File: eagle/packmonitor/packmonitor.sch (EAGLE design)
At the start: 35 parts, among them IC1 24C64, IC2 TCA4311A, IC3 AP2411, IC4 ACS712, Q1 PCHAN, X1 JST-XH-06-PIN-LONG-PAD

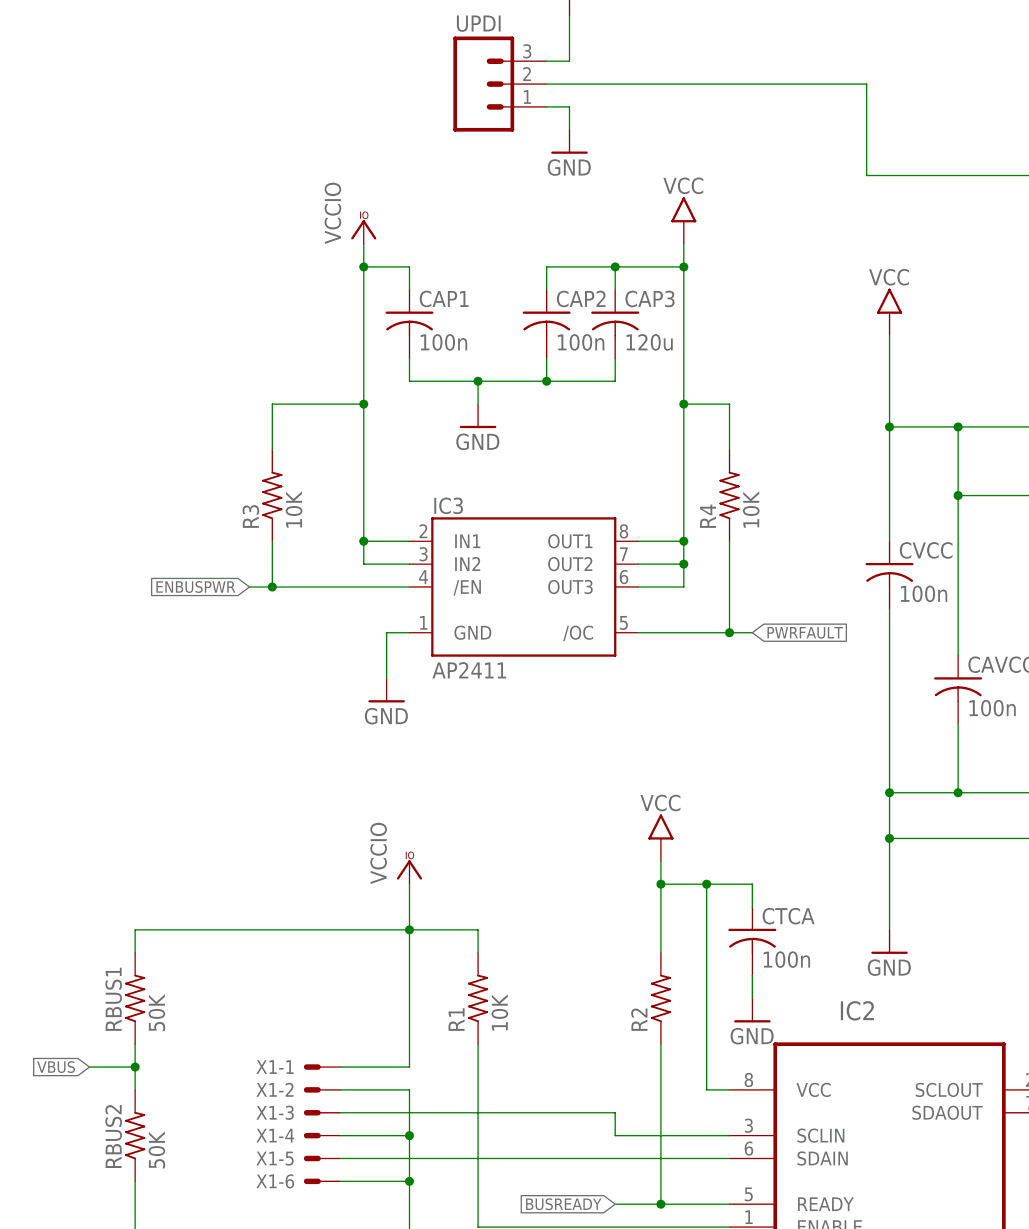
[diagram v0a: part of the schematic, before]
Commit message: got rid of input power switch
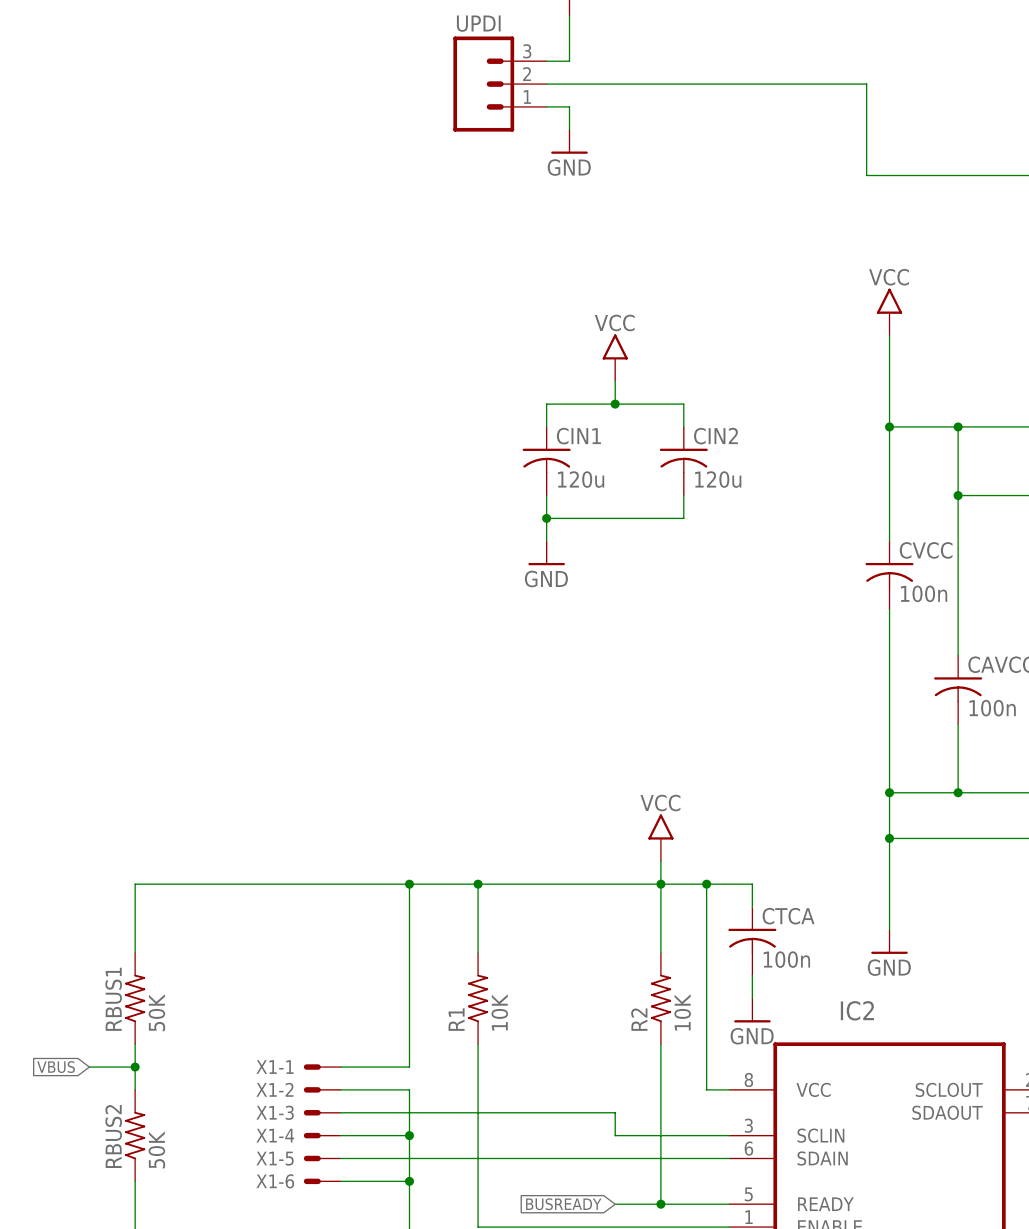
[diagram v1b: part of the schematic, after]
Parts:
- removed CAP1, CAP2: 100n, rcl:C-USC0603
- removed CAP3: 120u, rcl:C-USC1206
- removed IC3: AP2411, ti-special:TPS2041BD
- removed R3, R4: 10K, rcl:R-US_R0603
- added CIN1, CIN2: 120u, rcl:C-USC1206
- R2: value (none) -> 10K
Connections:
- removed net ENBUSPWR: IC3./EN, R3.1
- removed net PWRFAULT: IC3./OC, R4.1
- removed net VCCIO: CAP1.1, IC3.IN1, IC3.IN2, R1.2, R3.2, RBUS1.2, X1-1.S
- net GND: now also CIN1.2, CIN2.2; no longer CAP1.2, CAP2.2, CAP3.2, IC3.GND
- net VCC: now also CIN1.1, CIN2.1, R1.2, RBUS1.2, X1-1.S; no longer CAP2.1, CAP3.1, IC3.OUT1, IC3.OUT2, IC3.OUT3, R4.2

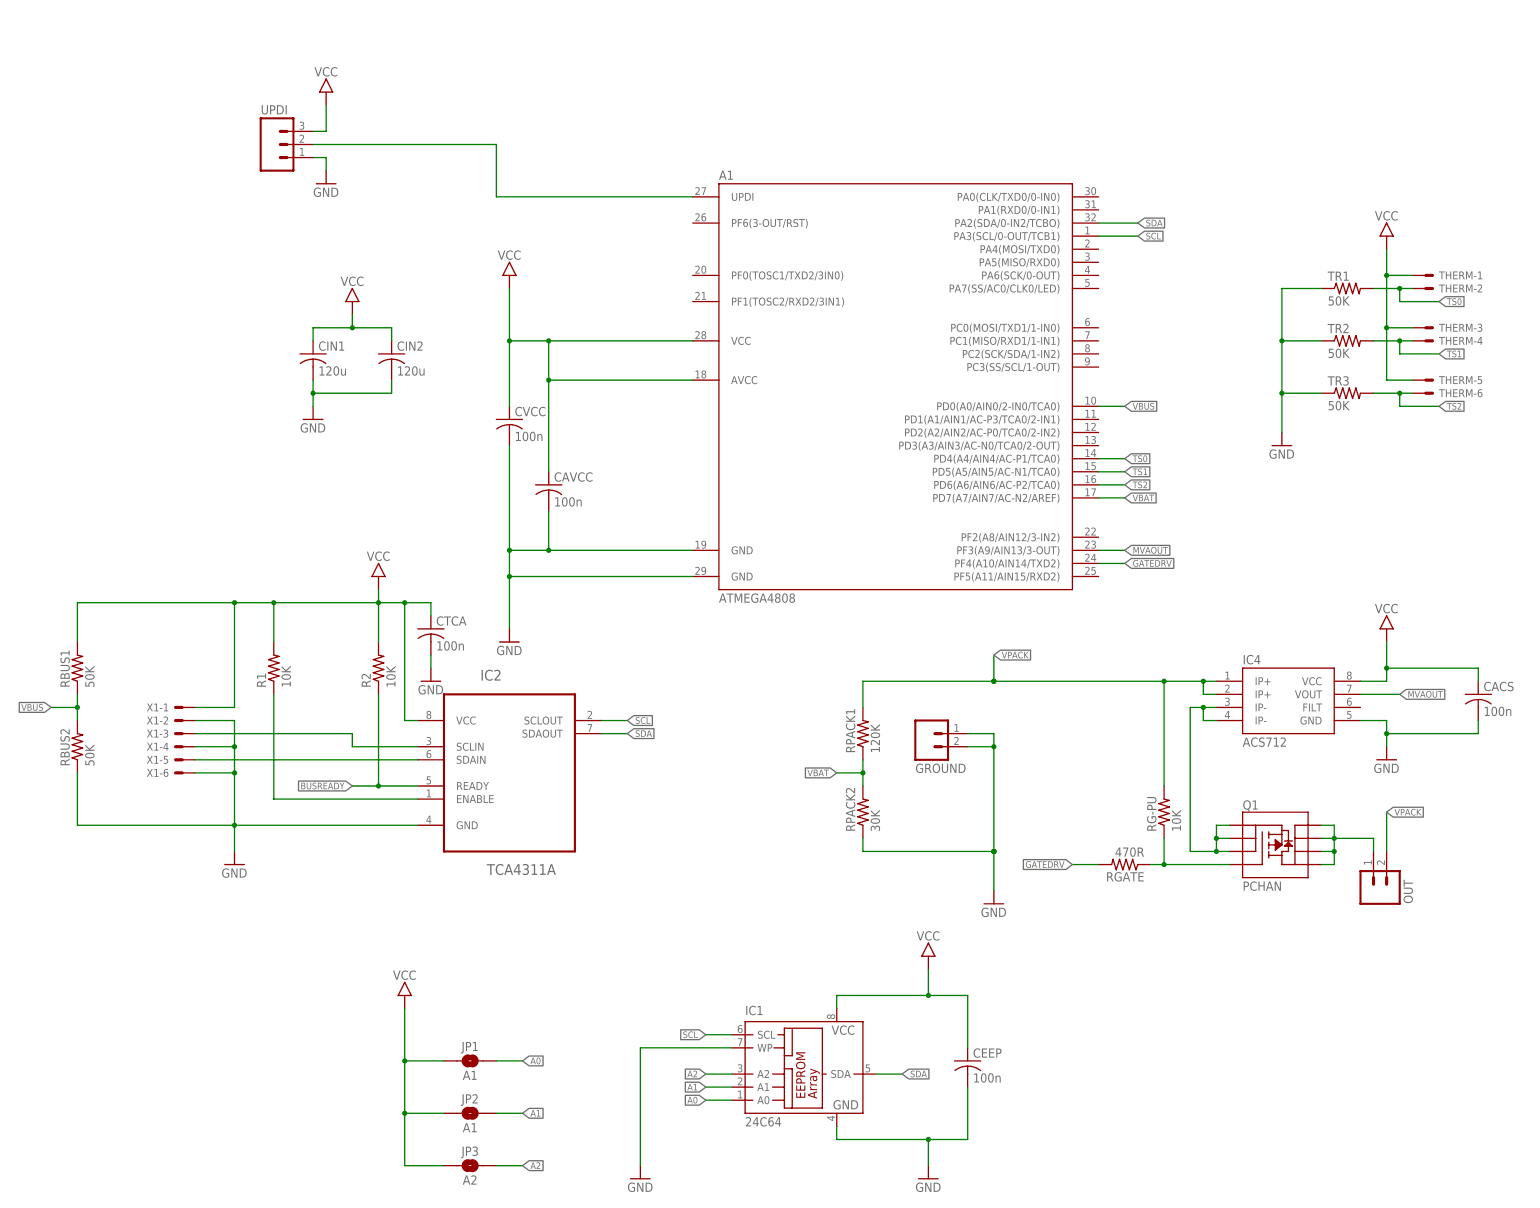
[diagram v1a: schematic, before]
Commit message: switched to avr128da32 chip & low side disconnect
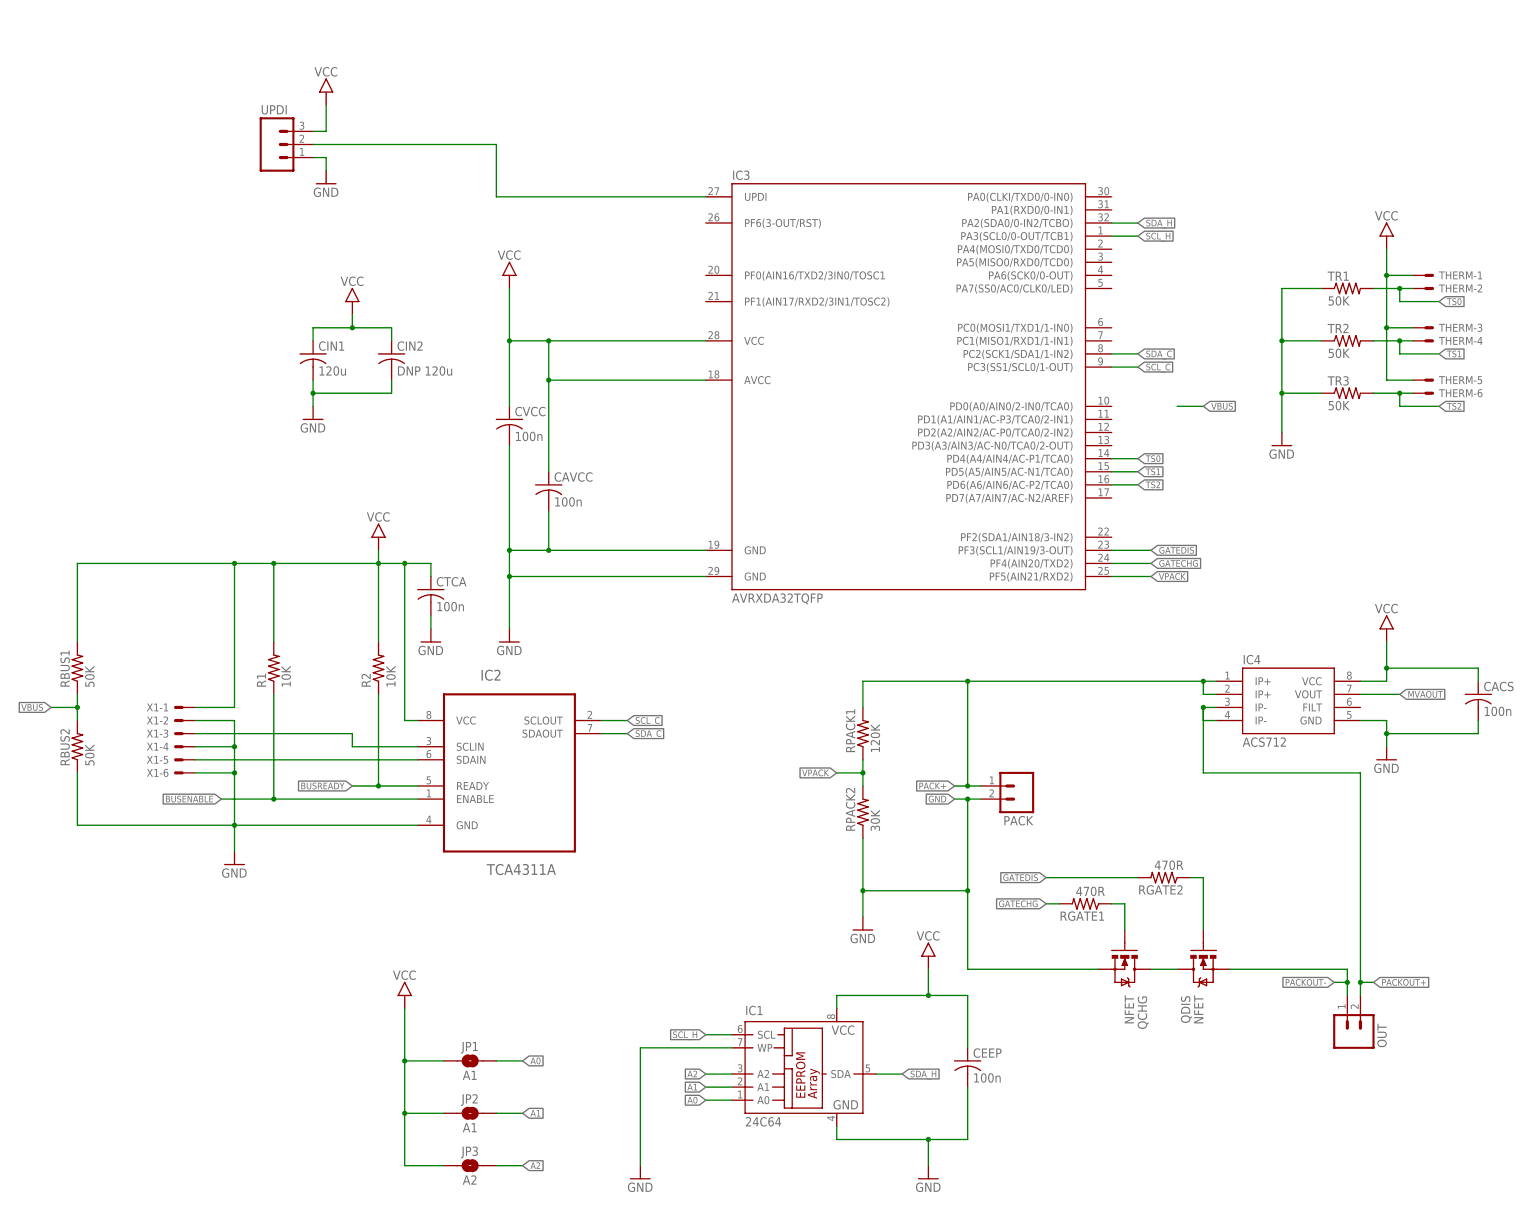
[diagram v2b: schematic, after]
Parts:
- removed A1: ATMEGA4808, microchip-special:ATMEGA4808-TQFN32A
- removed GROUND: (no value), SparkFun-Connectors:M023.5MM
- removed Q1: PCHAN, SparkFun-DiscreteSemi:MOSFET-PCHANNEL-SOIC8SOIC8
- removed RG-PU: 10K, rcl:R-US_R0603
- removed RGATE: 470R, rcl:R-US_R0603
- added IC3: AVRXDA32TQFP, microchip-special:AVRXDA32TQFP
- added PACK: (no value), SparkFun-Connectors:M023.5MM
- added QCHG, QDIS: NFET, SparkFun-DiscreteSemi:MOSFET-NCHANNELFDS6630A
- added RGATE1, RGATE2: 470R, rcl:R-US_R0603
- CIN2: value 120u -> DNP 120u
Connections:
- net N$6 renamed BUSENABLE
- removed net GATE: Q1.G, RG-PU.1, RGATE.1
- removed net GATEDRV: A1.PF4(A10/AIN14/TXD2), RGATE.2
- removed net P+IN: IC4.IP-@3, IC4.IP-@4, Q1.S@1, Q1.S@2, Q1.S@3
- removed net P+OUT: OUT.1, Q1.D@1, Q1.D@2, Q1.D@3, Q1.D@4
- removed net SCL: A1.PA3(SCL/0-OUT/TCB1), IC1.SCL, IC2.SCLOUT
- removed net SDA: A1.PA2(SDA/0-IN2/TCBO), IC1.SDA, IC2.SDAOUT
- removed net VBAT: A1.PD7(A7/AIN7/AC-N2/AREF), RPACK1.1, RPACK2.2
- new net GATECHG: IC3.PF4(AIN20/TXD2), RGATE1.2
- new net GATEDIS: IC3.PF3(SCL1/AIN19/3-OUT), RGATE2.2
- new net N$1: QCHG.G, RGATE1.1
- new net N$2: QDIS.G, RGATE2.1
- new net PACK+: IC4.IP+@1, IC4.IP+@2, PACK.1, RPACK1.2
- new net PACKOUT+: IC4.IP-@3, IC4.IP-@4, OUT.2
- new net PACKOUT-: OUT.1, QDIS.S
- new net PDISC: QCHG.D, QDIS.D
- new net SCL_C: IC2.SCLOUT, IC3.PC3(SS1/SCL0/1-OUT)
- new net SCL_H: IC1.SCL, IC3.PA3(SCL0/0-OUT/TCB1)
- new net SDA_C: IC2.SDAOUT, IC3.PC2(SCK1/SDA1/1-IN2)
- new net SDA_H: IC1.SDA, IC3.PA2(SDA0/0-IN2/TCBO)
- net GND: now also IC3.GND@1, IC3.GND@2, PACK.2, QCHG.S; no longer A1.GND@1, A1.GND@2, GROUND.1, GROUND.2
- net MVAOUT: no longer A1.PF3(A9/AIN13/3-OUT)
- net TS0: now also IC3.PD4(A4/AIN4/AC-P1/TCA0); no longer A1.PD4(A4/AIN4/AC-P1/TCA0)
- net TS1: now also IC3.PD5(A5/AIN5/AC-N1/TCA0); no longer A1.PD5(A5/AIN5/AC-N1/TCA0)
- net TS2: now also IC3.PD6(A6/AIN6/AC-P2/TCA0); no longer A1.PD6(A6/AIN6/AC-P2/TCA0)
- net UPDI: now also IC3.UPDI; no longer A1.UPDI
- net VBUS: no longer A1.PD0(A0/AIN0/2-IN0/TCA0)
- net VCC: now also IC3.AVCC, IC3.VCC; no longer A1.AVCC, A1.VCC
- net VPACK: now also IC3.PF5(AIN21/RXD2), RPACK1.1, RPACK2.2; no longer IC4.IP+@1, IC4.IP+@2, OUT.2, RG-PU.2, RPACK1.2
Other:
- moved on the sheet: CTCA, OUT

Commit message: layout and routing complete, needs fine tuning
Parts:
- removed JP1, JP2: A1, SparkFun-Jumpers:JUMPER-SMT_2_NO_SILK
- removed JP3: A2, SparkFun-Jumpers:JUMPER-SMT_2_NO_SILK
- removed R1, R2: 10K, rcl:R-US_R0603
- added RENAPD: 10K, rcl:R-US_R0603
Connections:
- net N$3 renamed SDAIN
- net N$4 renamed SCLIN
- removed net A0: IC1.A0, JP1.2
- removed net A1: IC1.A1, JP2.2
- removed net A2: IC1.A2, JP3.2
- net BUSENABLE: now also IC3.PD2(A2/AIN2/AC-P0/TCA0/2-IN2), RENAPD.2; no longer R1.1
- net BUSREADY: now also IC3.PD1(A1/AIN1/AC-P3/TCA0/2-IN1); no longer R2.1
- net GND: now also IC1.A0, IC1.A1, IC1.A2, IC4.FILT, RENAPD.1; no longer X1-2.S
- net MVAOUT: now also IC3.PF1(AIN17/RXD2/3IN1/TOSC2)
- net VBUS: now also IC3.PD0(A0/AIN0/2-IN0/TCA0)
- net VCC: now also X1-2.S; no longer JP1.1, JP2.1, JP3.1, R1.2, R2.2
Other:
- moved on the sheet: CEEP, IC1

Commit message: final tweaks, fingers crossed order sent
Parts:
- added CACS1: 1n, rcl:C-USC0603
- renumbered CACS to CACS2, RENAPD to RENA, X1 to HOST_BUS
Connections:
- new net N$3: CACS1.1, IC4.FILT
- net GND: now also CACS1.2; no longer IC4.FILT
